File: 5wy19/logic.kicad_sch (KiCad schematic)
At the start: 25 parts, among them Q1 BC846, Q2 BC846, Q28 BCR183, Q5 BAW56, Q6 BAW56, Q8 BC846, Q9 BC846, U1 74HC32

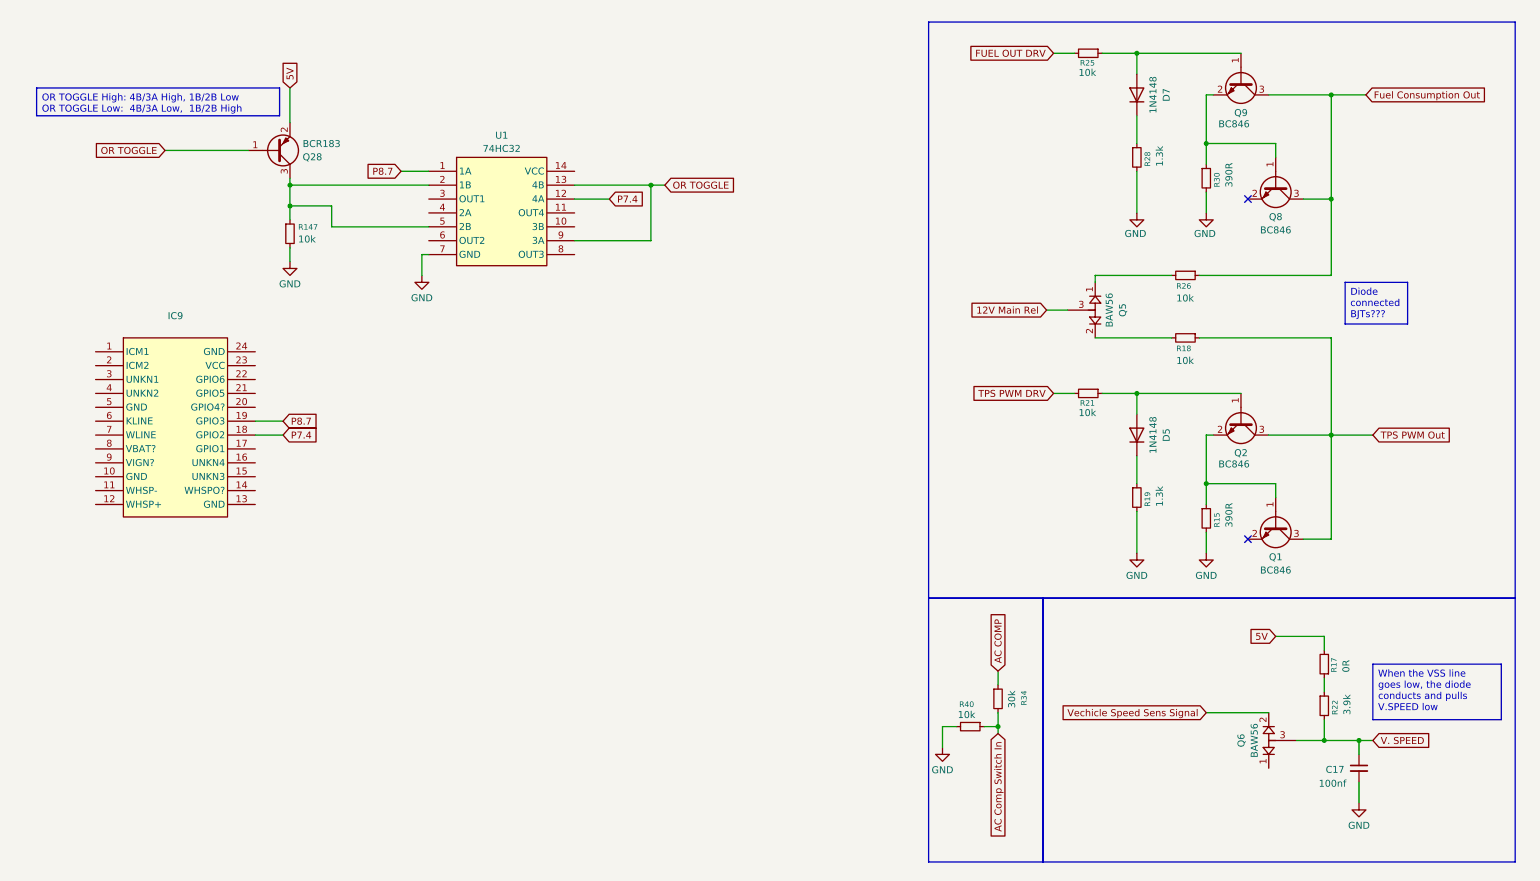
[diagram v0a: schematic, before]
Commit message: Further progress on MCU and connected circuits
Mostly sensors, knock control, some pins from the IO drivers and the unknown AMIS chip
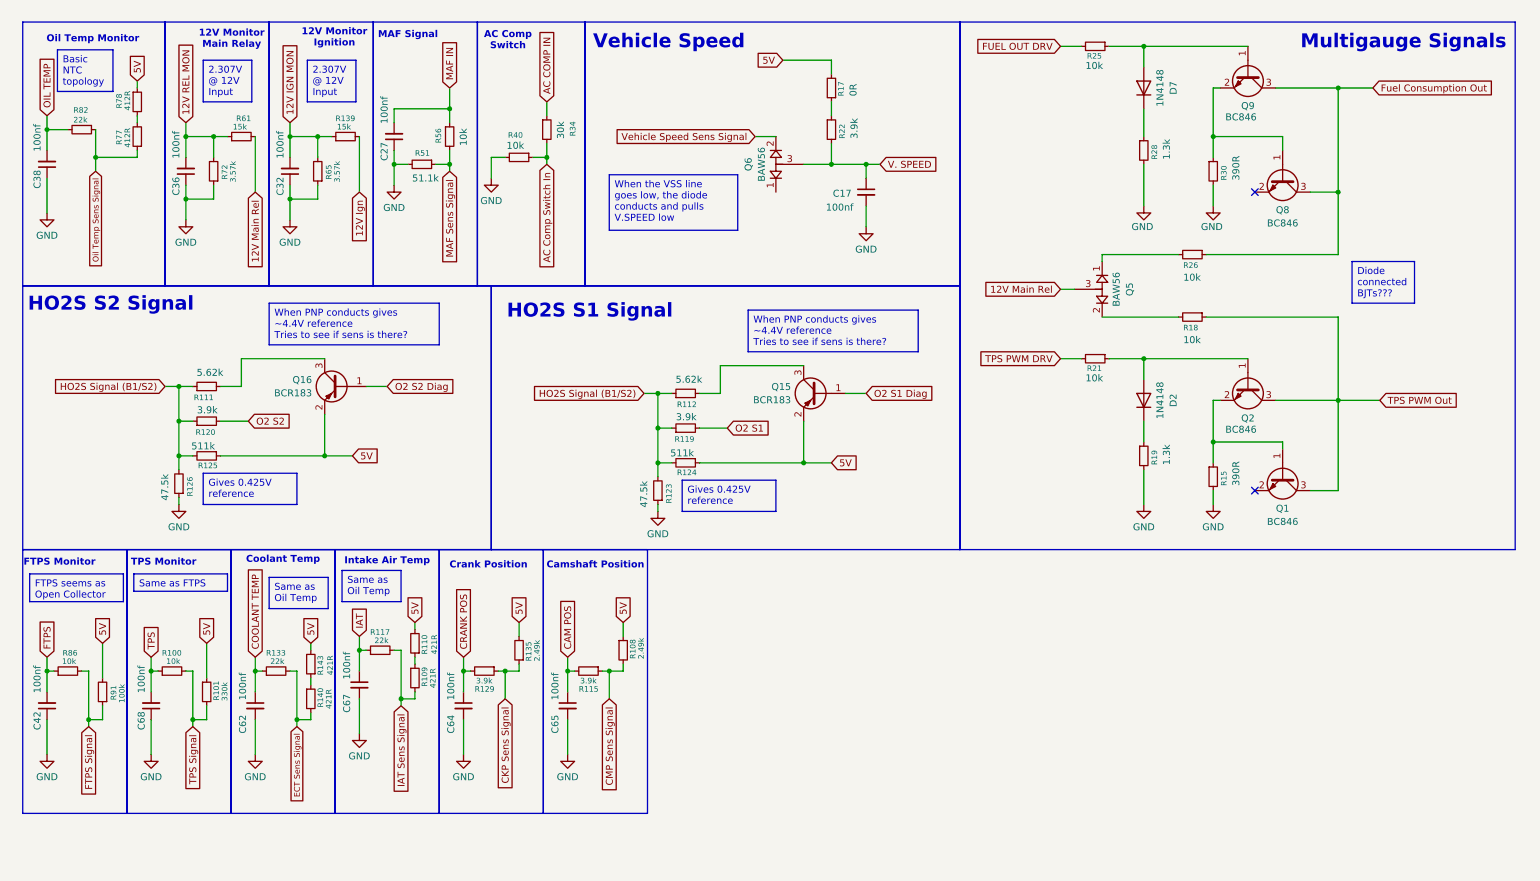
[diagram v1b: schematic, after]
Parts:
- removed IC9: ~, symbol SIMK43:0504TAK
- removed Q28: BCR183, Package_TO_SOT_SMD:SOT-23, symbol Transistor_BJT:BC807
- removed R147: 10k, symbol Device:R_Small
- removed U1: 74HC32, symbol SIMK43:74HC32
- added C27, C32, C36, C38, C42, C62, C64, C65, C67, C68: 100nf, symbol Device:C_Small
- added Q15, Q16: BCR183, Package_TO_SOT_SMD:SOT-23, symbol Transistor_BJT:BC807
- added R100, R56, R86: 10k, symbol Device:R_Small
- added R101: 330k, symbol Device:R_Small
- added R108, R135: 2.49k, symbol Device:R_Small
- added R109, R110, R140, R143: 421R, symbol Device:R_Small
- added R111, R112: 5.62k, symbol Device:R_Small
- added R115, R119, R120, R129: 3.9k, symbol Device:R_Small
- added R117, R133, R82: 22k, symbol Device:R_Small
- added R123, R126: 47.5k, symbol Device:R_Small
- added R124, R125: 511k, symbol Device:R_Small
- added R139, R61: 15k, symbol Device:R_Small
- added R51: 51.1k, symbol Device:R_Small
- added R65, R72: 3.57k, symbol Device:R_Small
- added R77, R78: 412R, symbol Device:R_Small
- added R91: 100k, symbol Device:R_Small
- renumbered D5 to D2
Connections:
- net 12V Main Rel: now also R61.2
- net 5V: now also Q15.2 (E), Q16.2 (E), R101.1, R108.1, R110.2, R124.1, R125.1, R135.2, R143.2, R78.1, R91.2
- net GND: now also C27.1, C32.1, C36.1, C38.1, C42.1, C62.2, C64.2, C65.2, C67.2, C68.1, R123.1, R126.1, R51.2, R65.1, R72.1
- net AC COMP renamed AC COMP IN
- net Vechicle Speed Sens Signal renamed Vehicle Speed Sens Signal
- new net: Q15.3 (C), R112.2
- new net: R77.2, R78.2
- new net: R140.1, R143.1
- new net: R109.1, R110.1
- new net: Q16.3 (C), R111.2
- new net 12V IGN MON: C32.2, R139.1, R65.2
- new net 12V Ign: R139.2
- new net 12V REL MON: C36.2, R61.1, R72.2
- new net CAM POS: C65.1, R115.2
- new net CKP Sens Signal: R129.1, R135.1
- new net CMP Sens Signal: R108.2, R115.1
- new net COOLANT TEMP: C62.1, R133.1
- new net CRANK POS: C64.1, R129.2
- new net ECT Sens Signal: R133.2, R140.2
- new net FTPS: C42.2, R86.1
- new net FTPS Signal: R86.2, R91.1
- new net HO2S Signal (B1/S2): R111.1, R112.1, R119.1, R120.1, R123.2, R124.2, R125.2, R126.2
- new net IAT: C67.1, R117.1
- new net IAT Sens Signal: R109.2, R117.2
- new net MAF IN: C27.2, R56.1
- new net MAF Sens Signal: R51.1, R56.2
- new net O2 S1: R119.2
- new net O2 S1 Diag: Q15.1 (B)
- new net O2 S2: R120.2
- new net O2 S2 Diag: Q16.1 (B)
- new net OIL TEMP: C38.2, R82.2
- new net Oil Temp Sens Signal: R77.1, R82.1
- new net TPS: C68.2, R100.1
- new net TPS Signal: R100.2, R101.2
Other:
- note added: "12V Monitor Ignition"
- note added: "12V Monitor Main Relay"
- note added: "AC Comp Switch"
- note added: "Camshaft Position"
- note added: "Coolant Temp"
- note added: "Crank Position"
- note added: "FTPS Monitor"
- note added: "HO2S S1 Signal"
- note added: "HO2S S2 Signal"
- note added: "Intake Air Temp"
- note added: "MAF Signal"
- note added: "Multigauge Signals"
- note added: "Oil Temp Monitor"
- note added: "TPS Monitor"
- note added: "Vehicle Speed"
- moved on the sheet: C17, D2, D7, Q1, Q2, Q5, Q6, Q8, Q9, R15, R17, R18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
